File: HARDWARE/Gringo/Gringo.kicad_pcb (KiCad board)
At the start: 2 copper layers, 7 parts, among them J1 Conn_01x06, J3 Conn_01x06, J4 Alim, J5 Conn_01x06, J6 Conn_01x06, J7 Conn_01x06, U2 BQ500212ARGZT

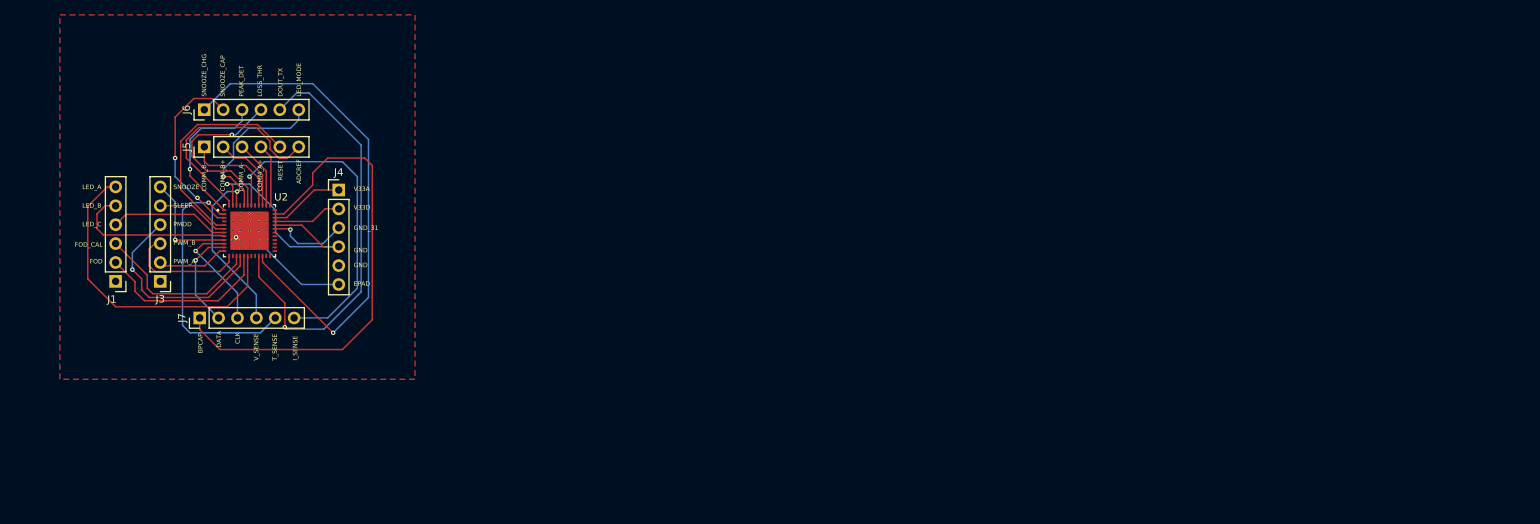
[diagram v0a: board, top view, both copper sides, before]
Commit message: PCB test Marius - 3 composants faits
Potentiellement rajouter certains composants avant de le commander (je vais laisser faire MARIUS)
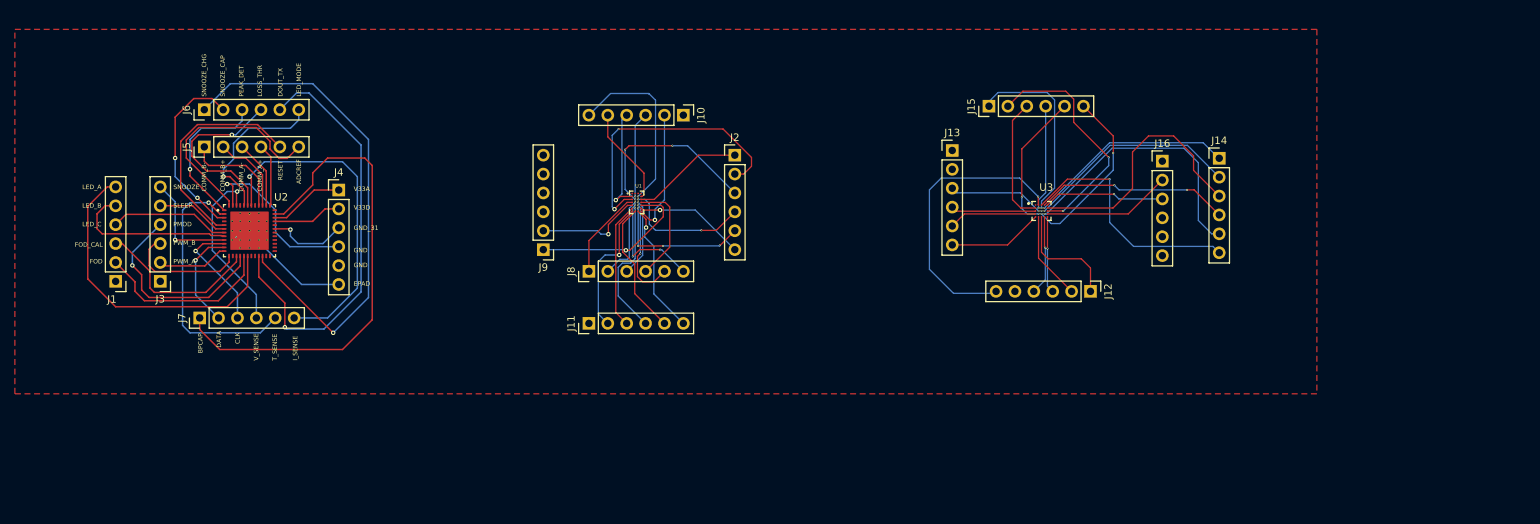
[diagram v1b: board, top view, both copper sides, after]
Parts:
- added J10: Conn_01x06, Connector_PinHeader_2.54mm:PinHeader_1x06_P2.54mm_Vertical, F.Cu at (130.3, 60.7)
- added J11: Conn_01x06, Connector_PinHeader_2.54mm:PinHeader_1x06_P2.54mm_Vertical, F.Cu at (117.6, 88.7)
- added J12: Conn_01x06, Connector_PinHeader_2.54mm:PinHeader_1x06_P2.54mm_Vertical, F.Cu at (185.1, 84.4)
- added J13: Conn_01x06, Connector_PinHeader_2.54mm:PinHeader_1x06_P2.54mm_Vertical, F.Cu at (166.5, 65.5)
- added J14: Conn_01x06, Connector_PinHeader_2.54mm:PinHeader_1x06_P2.54mm_Vertical, F.Cu at (202.4, 66.5)
- added J15: Conn_01x06, Connector_PinHeader_2.54mm:PinHeader_1x06_P2.54mm_Vertical, F.Cu at (171.4, 59.5)
- added J16: Conn_01x06, Connector_PinHeader_2.54mm:PinHeader_1x06_P2.54mm_Vertical, F.Cu at (194.7, 66.9)
- added J2: Conn_01x06, Connector_PinHeader_2.54mm:PinHeader_1x06_P2.54mm_Vertical, F.Cu at (137.3, 66.1)
- added J8: Conn_01x06, Connector_PinHeader_2.54mm:PinHeader_1x06_P2.54mm_Vertical, F.Cu at (117.6, 81.7)
- added J9: Conn_01x06, Connector_PinHeader_2.54mm:PinHeader_1x06_P2.54mm_Vertical, F.Cu at (111.5, 78.8)
- added U1: BQ51003YFPT, BQ51003YFPT:BGA28N40P7X4_300X188X50N, F.Cu at (124.1, 72.5)
- added U3: BQ25120AYFPT, BQ25120AYFPT:IC_BQ25120AYFPT, F.Cu at (178.5, 73.6)
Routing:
- net Net-(J12-Pin_6): track 0.00 -> 38.6 mm, vias 0 -> 1
- net Net-(J2-Pin_2): track 0.00 -> 37.5 mm, vias 0 -> 2
- net Net-(J14-Pin_5): track 0.00 -> 36.5 mm, vias 0 -> 1
- net Net-(J14-Pin_3): track 0.00 -> 34.5 mm
- net Net-(J14-Pin_6): track 0.00 -> 32.8 mm, vias 0 -> 1
- net Net-(J15-Pin_2): track 0.00 -> 31.8 mm, vias 0 -> 2
- net Net-(J14-Pin_2): track 0.00 -> 28.9 mm, vias 0 -> 1
- net Net-(J14-Pin_1): track 0.00 -> 28.0 mm, vias 0 -> 1
- net Net-(J14-Pin_4): track 0.00 -> 26.2 mm, vias 0 -> 2
- net Net-(J15-Pin_1): track 0.00 -> 25.6 mm, vias 0 -> 1
- net Net-(J2-Pin_3): track 0.00 -> 24.8 mm, vias 0 -> 3
- net Net-(J10-Pin_6): track 0.00 -> 24.5 mm, vias 0 -> 1
- net Net-(J15-Pin_6): track 0.00 -> 23.4 mm, vias 0 -> 2
- net Net-(J9-Pin_1): track 0.00 -> 22.4 mm, vias 0 -> 1
- net Net-(J2-Pin_5): track 0.00 -> 18.9 mm, vias 0 -> 4
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
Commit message: Update the eval kit PCB with BPM module part
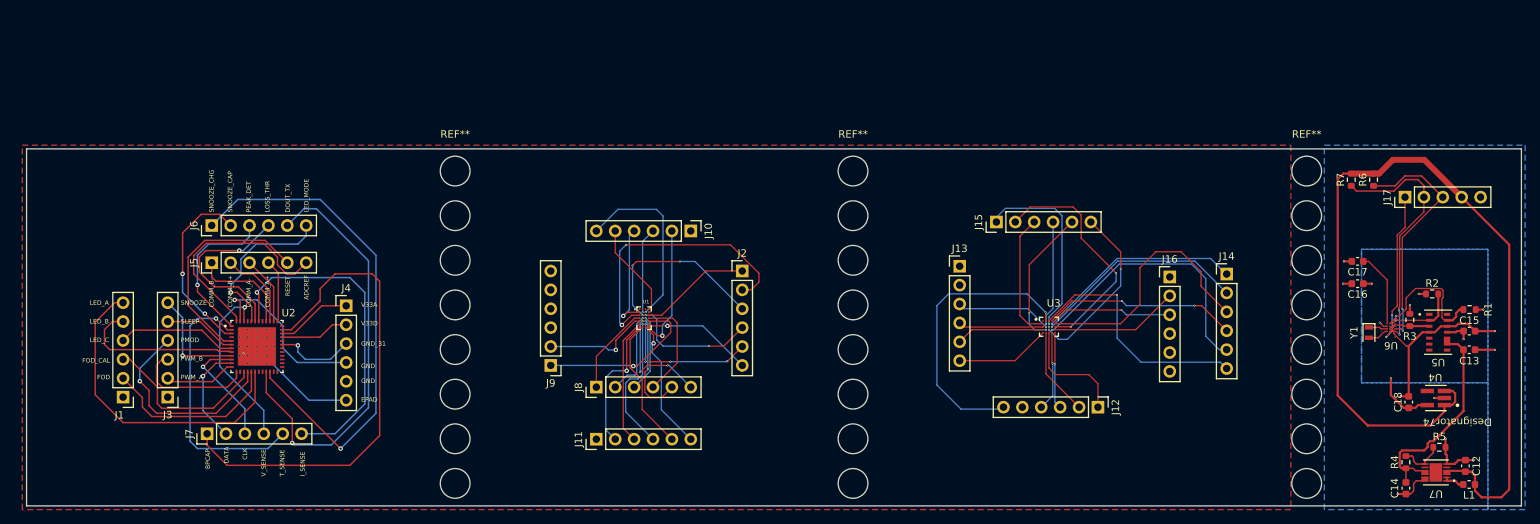
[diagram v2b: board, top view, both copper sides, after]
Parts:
- added ?: , , F.Cu at (214.2, 110.2)
- added ?: , , F.Cu at (153.2, 98.2)
- added ?: , , F.Cu at (214.2, 104.2)
- added ?: , , F.Cu at (153.2, 104.2)
- added ?: , , F.Cu at (99.7, 74.2)
- added ?: , , F.Cu at (153.2, 92.2)
- added ?: , , F.Cu at (214.2, 80.2)
- added ?: , , F.Cu at (99.7, 110.2)
- added ?: , , F.Cu at (153.2, 80.2)
- added ?: , , F.Cu at (99.7, 92.2)
- added ?: , , F.Cu at (214.2, 92.2)
- added ?: , , F.Cu at (214.2, 98.2)
- added ?: , , F.Cu at (99.7, 80.2)
- added ?: , , F.Cu at (214.2, 74.2)
- added ?: , , F.Cu at (99.7, 98.2)
- added ?: , , F.Cu at (214.2, 86.2)
- added ?: , , F.Cu at (153.2, 74.2)
- added ?: , , F.Cu at (99.7, 104.2)
- added ?: , , F.Cu at (153.2, 110.2)
- added ?: , , F.Cu at (153.2, 86.2)
- added ?: , , F.Cu at (99.7, 86.2)
- added C12: 10u, Capacitor_SMD:C_0603_1608Metric, F.Cu at (235.5, 107.9)
- added C13: 10u, Capacitor_SMD:C_0603_1608Metric, F.Cu at (236.0, 92.3)
- added C14: 22u, Capacitor_SMD:C_0603_1608Metric, F.Cu at (227.5, 110.9)
- added C15: 100n, Capacitor_SMD:C_0603_1608Metric, F.Cu at (236.0, 89.8)
- added C16: 1u, Capacitor_SMD:C_0603_1608Metric, F.Cu at (221.0, 83.4)
- added C17: 1u, Capacitor_SMD:C_0603_1608Metric, F.Cu at (221.0, 80.4)
- added C18: 1u, Capacitor_SMD:C_0603_1608Metric, F.Cu at (227.9, 99.3)
- added J17: Conn_01x05_Pin, Connector_PinHeader_2.54mm:PinHeader_1x05_P2.54mm_Vertical, F.Cu at (227.4, 71.8)
- added L1: 2u2, Inductor_SMD:L_0603_1608Metric, F.Cu at (236.0, 110.4)
- added R1: 4K7, Resistor_SMD:R_0603_1608Metric, F.Cu at (236.1, 86.9)
- added R2: 4K7, Resistor_SMD:R_0603_1608Metric, F.Cu at (231.0, 84.8)
- added R3: 4K7, Resistor_SMD:R_0603_1608Metric, F.Cu at (228.0, 88.3)
- added R4: 750K, Resistor_SMD:R_0603_1608Metric, F.Cu at (227.5, 107.4)
- added R5: 100K, Resistor_SMD:R_0603_1608Metric, F.Cu at (232.0, 105.4)
- added R6: 4K7, Resistor_SMD:R_0603_1608Metric, F.Cu at (223.1, 69.4)
- added R7: 4K7, Resistor_SMD:R_0603_1608Metric, F.Cu at (220.1, 69.4)
- added REF**: MountingHole_4mm, MountingHole:MountingHole_4mm, F.Cu at (153.2, 68.2)
- added REF**: MountingHole_4mm, MountingHole:MountingHole_4mm, F.Cu at (214.2, 68.2)
- added REF**: MountingHole_4mm, MountingHole:MountingHole_4mm, F.Cu at (99.7, 68.2)
- added U4: PTPS7A2018PDBVR, PTPS7A2018PDBVR:DBV0005A-IPC_A, F.Cu at (231.5, 98.8)
- added U5: MAX30101EFD+, MAX30101EFD:21-1048_F143A5&plus_1_MXM-M, F.Cu at (231.8, 89.9)
- added U6: MAX32664GWEA+T, MAX32664GWEA-T:21-100241A_W161K1&plus_1_MXM, F.Cu at (225.5, 89.3)
- added U7: PAM2401YPADJ, PAM2401YPADJ:SON12_U-DFN3030-12_DIO-M, F.Cu at (231.5, 108.8)
- added Y1: 32k768, Crystal:Crystal_SMD_2012-2Pin_2.0x1.2mm, F.Cu at (222.5, 90.0)
- moved J1 15.6 mm to (55.0, 98.7)
- moved J10 15.6 mm to (131.3, 76.3)
- moved J11 15.6 mm to (118.6, 104.3)
- moved J2 15.6 mm to (138.3, 81.7)
- moved J3 15.6 mm to (61.0, 98.7)
- moved J4 15.6 mm to (85.0, 86.4)
- moved J8 15.6 mm to (118.6, 97.3)
- moved J9 15.6 mm to (112.5, 94.4)
- moved U2 15.6 mm to (73.0, 91.8)
- moved U3 15.6 mm to (179.5, 89.2)
- moved J12 15.6 mm to (186.1, 100.0)
- moved J13 15.6 mm to (167.5, 81.0)
- moved J14 15.6 mm to (203.4, 82.1)
- moved J15 15.6 mm to (172.4, 75.1)
- moved J16 15.6 mm to (195.7, 82.5)
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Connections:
- J3 pad 2: Net-(J3-Pin_2) -> unconnected-(J3-Pin_2-Pad2)
- J3 pad 3: Net-(J3-Pin_3) -> unconnected-(J3-Pin_3-Pad3)
- J3 pad 5: Net-(J3-Pin_5) -> Net-(J3-Pin_4)
- U1 pad C1: Net-(J2-Pin_2) -> Net-(U1-BOOT2)
- U1 pad C4: Net-(J2-Pin_1) -> Net-(U1-BOOT1)
- U1 pad E1: Net-(J9-Pin_2) -> Net-(U1-COMM2)
- U1 pad E2: Net-(J8-Pin_6) -> Net-(U1-CLAMP2)
- U1 pad E3: Net-(J8-Pin_5) -> Net-(U1-CLAMP1)
- U1 pad E4: Net-(J9-Pin_1) -> Net-(U1-COMM1)
- U2 pad 12: Net-(J3-Pin_2) -> unconnected-(U2-PWM_A-Pad12)
- U2 pad 13: Net-(J3-Pin_3) -> unconnected-(U2-PWM_B-Pad13)
- U2 pad 6: Net-(J3-Pin_5) -> Net-(J3-Pin_4)
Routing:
- net +3.3V: track 0.00 -> 124.3 mm
- net GND: track 23.8 -> 67.2 mm, vias 1 -> 10
- net HOST_SCL: track 0.00 -> 33.2 mm, vias 0 -> 2
- net HOST_SDA: track 0.00 -> 32.5 mm, vias 0 -> 2
- net +5V: track 0.00 -> 29.3 mm
- net (no net): track 0.00 -> 26.3 mm
- net RST: track 0.00 -> 20.9 mm, vias 0 -> 2
- net HR_INT: track 0.00 -> 17.8 mm, vias 0 -> 2
- net +1V8: track 0.00 -> 16.9 mm, vias 0 -> 7
- net Net-(J3-Pin_3): track 16.7 -> 0.00 mm
- net Net-(U2-VCORE): track 0.00 -> 10.1 mm
- net SSR_SCL: track 0.00 -> 10.1 mm
- net Net-(J3-Pin_5): track 9.88 -> 0.00 mm
- net Net-(J3-Pin_4): track 27.6 -> 37.5 mm
- net Net-(J3-Pin_2): track 9.61 -> 0.00 mm
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- added copper zone on B.Cu, net +1V8
- added copper zone on B.Cu, net GND
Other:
- board outline added: 201 x 48 mm

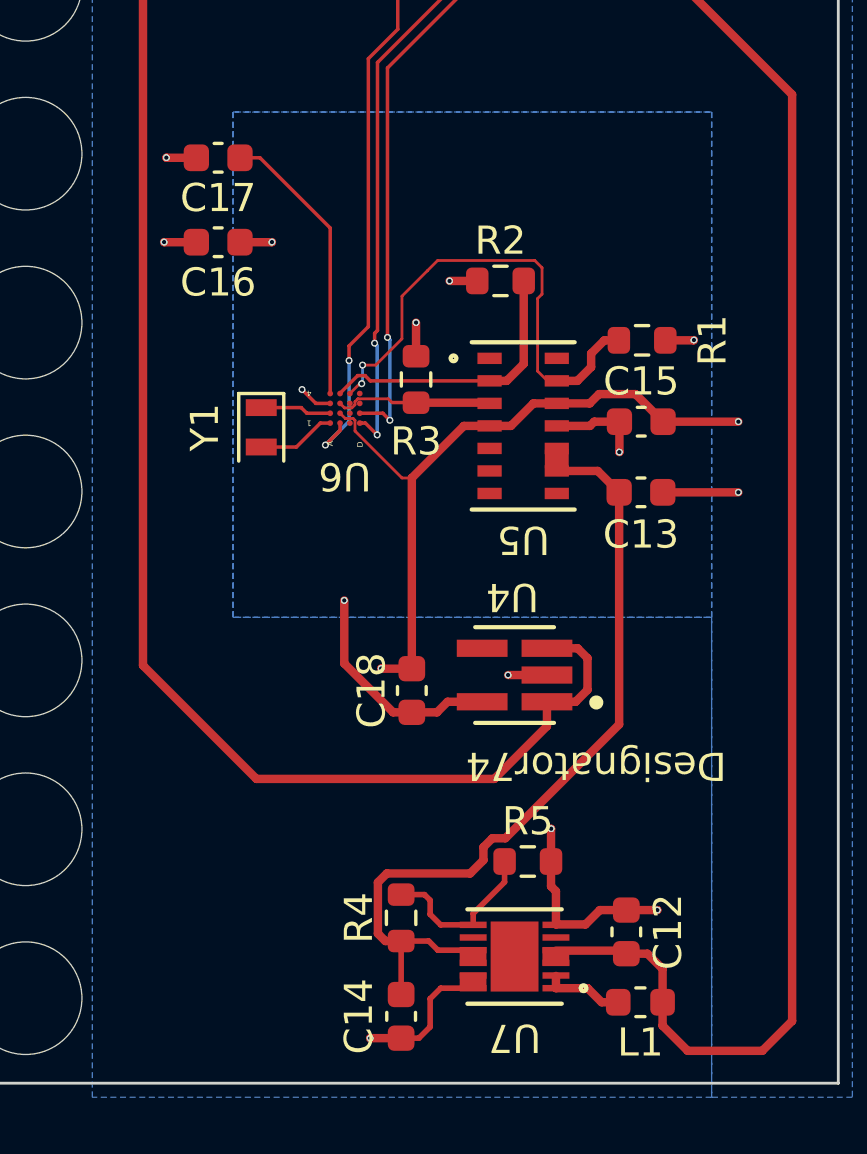
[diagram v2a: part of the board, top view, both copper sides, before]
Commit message: Update the eval kit PCB and production files
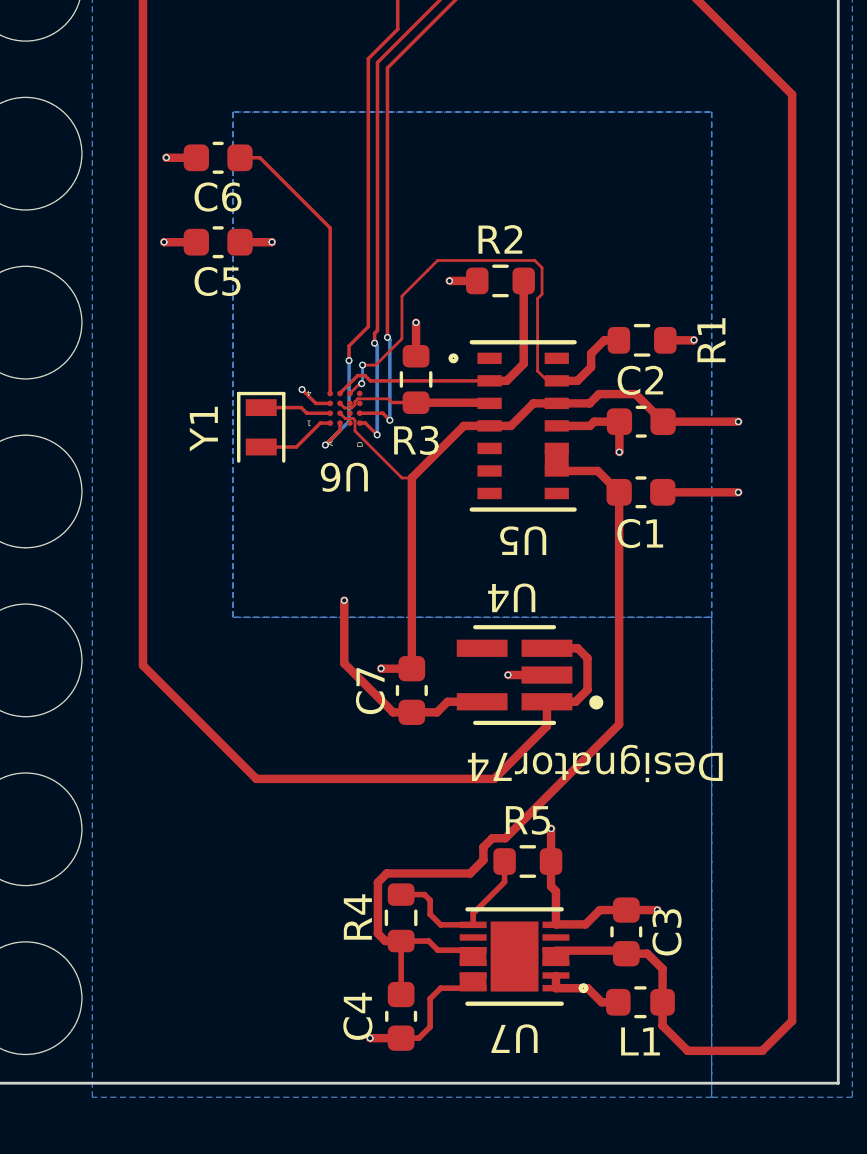
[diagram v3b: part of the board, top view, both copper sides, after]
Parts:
- renumbered C13 to C1, C15 to C2, C12 to C3, C14 to C4, C16 to C5, C17 to C6, C18 to C7
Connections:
- J10 pad 6: Net-(J10-Pin_6) -> Net-(J10-Pin_4)
- U1 pad B3: Net-(J10-Pin_6) -> Net-(J10-Pin_4)
- U1 pad C1: Net-(U1-BOOT2) -> Net-(J2-Pin_2)
- U1 pad C4: Net-(U1-BOOT1) -> Net-(J2-Pin_1)
- U1 pad E1: Net-(U1-COMM2) -> Net-(J9-Pin_2)
- U1 pad E2: Net-(U1-CLAMP2) -> Net-(J8-Pin_6)
- U1 pad E3: Net-(U1-CLAMP1) -> Net-(J8-Pin_5)
- U1 pad E4: Net-(U1-COMM1) -> Net-(J9-Pin_1)
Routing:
- net Net-(J10-Pin_6): track 24.5 -> 0.00 mm, vias 1 -> 0
- net Net-(J10-Pin_4): track 14.4 -> 38.9 mm, vias 1 -> 2
